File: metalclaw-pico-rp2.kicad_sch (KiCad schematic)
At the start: 115 parts, among them J1 USB_C_Receptacle_USB2.0_14P, J2 Conn_02x05_Odd_Even, SW1 SW_Push, SW2 SW_Push, U1 XC6220B331MR, U2 RP2354B, U3 APS6404L-3SQRx-SN, Y1 XRCGB40M000F1S2FR0

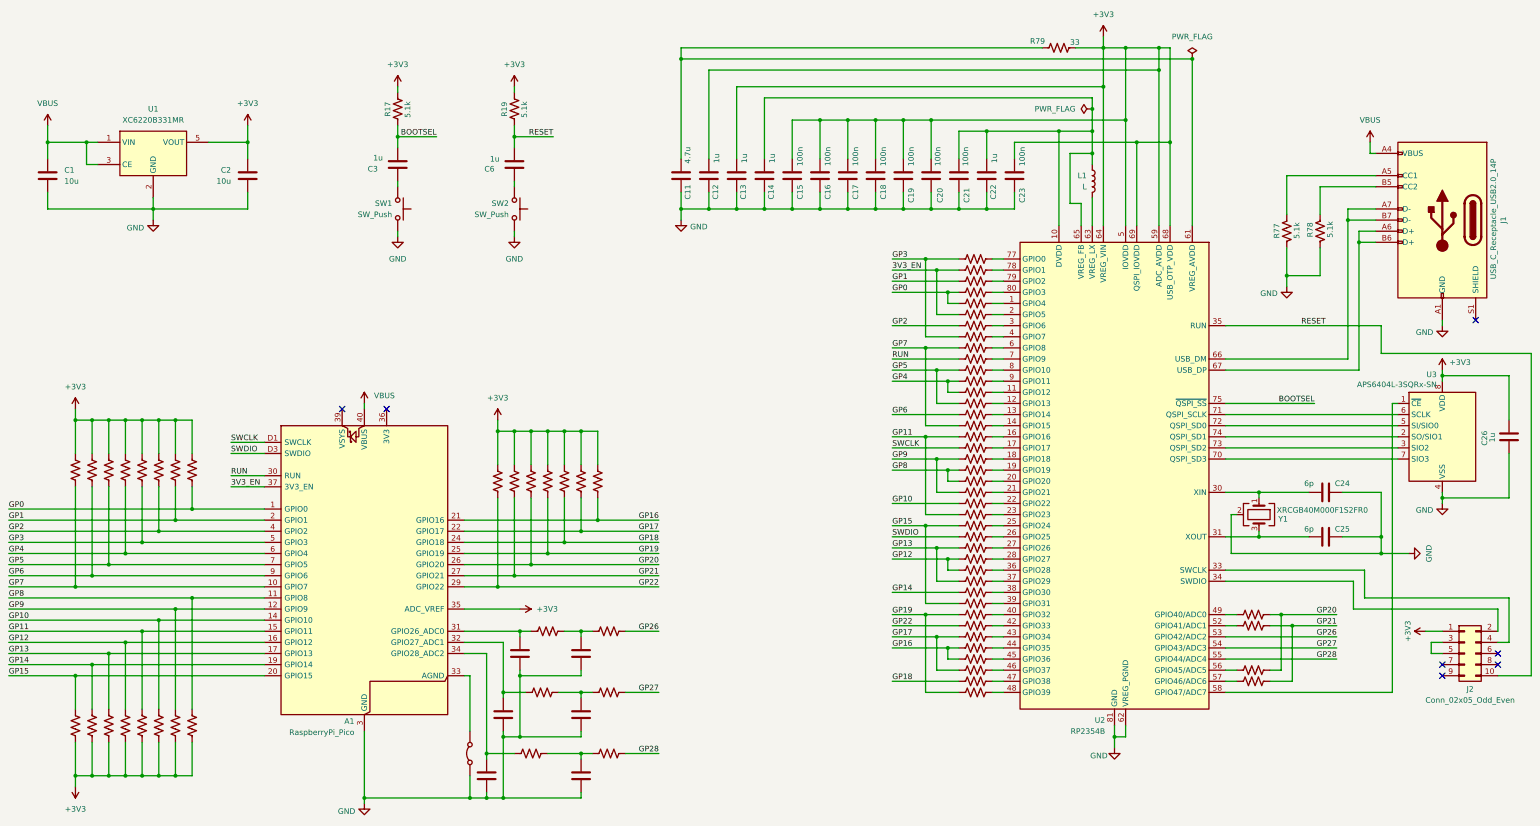
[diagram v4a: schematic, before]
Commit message: Fix power supply connections
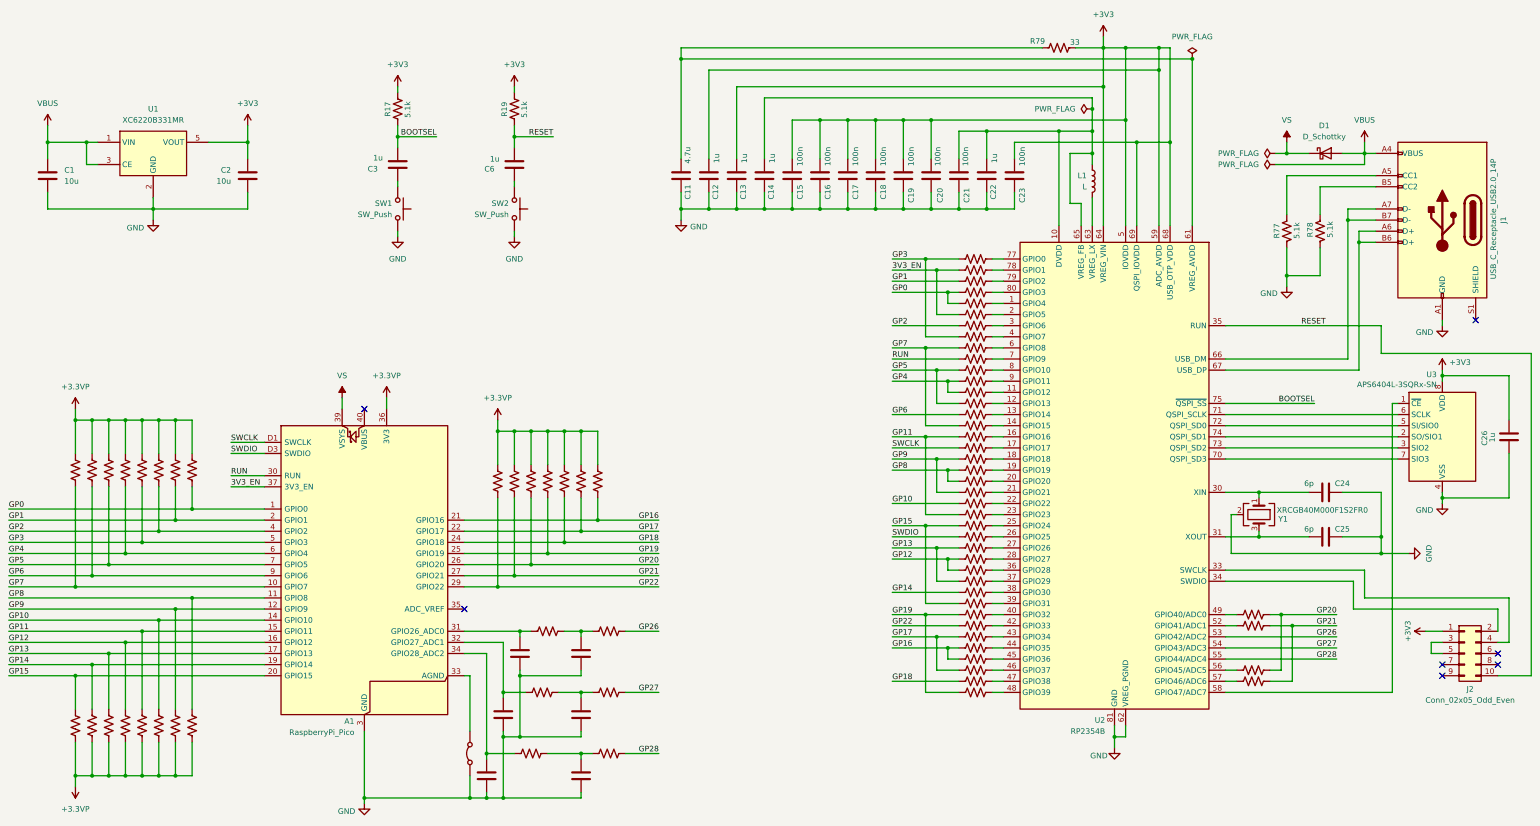
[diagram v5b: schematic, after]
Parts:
- added D1: D_Schottky, symbol Device:D_Schottky
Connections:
- net +3V3: no longer A1.35 (ADC_VREF), R1.2, R10.1, R11.2, R12.1, R13.2, R14.1, R15.2, R16.1, R18.2, R2.1, R20.2, R21.2, R24.2, R26.2, R27.2, R28.2, R3.2, R4.1, R5.2, R6.1, R7.2, R8.1, R9.2
- net VBUS: now also D1.2 (A); no longer A1.40 (VBUS)
- net +3.3VP: now reaches A1.36 (3V3)
- net +3.3VP: now also R1.2, R10.1, R11.2, R12.1, R13.2, R14.1, R15.2, R16.1, R18.2, R2.1, R20.2, R21.2, R24.2, R26.2, R27.2, R28.2, R3.2, R4.1, R5.2, R6.1, R7.2, R8.1, R9.2
- net VS: now reaches A1.39 (VSYS)
- net VS: now also D1.1 (K)

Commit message: Add pull-up for PSRAM chip-select
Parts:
- added R76: 220, Resistor_SMD:R_0201_0603Metric, symbol Device:R_US
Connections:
- net +3V3: now also R76.2
- net at U2.58 (GPIO47/ADC7), U3.1 (~{CE}): now also R76.1
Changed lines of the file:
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@@
 	)
 	(junction
+		(at 353.06 196.85)
+		(diameter 0)
+		(color 0 0 0 0)
+	)
+	(junction
 		(at 241.3 66.04)
 		(diameter 0)
@@
 	(wire
 		(pts
+			(xy 353.06 196.85) (xy 359.41 196.85)
+		)
+		(stroke
+			(width 0)
+			(type default)
+		)
+	)
+	(wire
+		(pts
 			(xy 255.27 184.15) (xy 245.11 184.15)
 		)
@@
 	(wire
 		(pts
+			(xy 353.06 185.42) (xy 353.06 186.69)
+		)
+		(stroke
+			(width 0)
+			(type default)
+		)
+	)
+	(wire
+		(pts
 			(xy 347.98 151.13) (xy 356.87 151.13)
 		)
@@
 	(wire
 		(pts
+			(xy 353.06 194.31) (xy 353.06 196.85)
+		)
+		(stroke
+			(width 0)
+			(type default)
+		)
+	)
+	(wire
+		(pts
 			(xy 73.66 182.88) (xy 73.66 200.66)
 		)
@@
 	(wire
 		(pts
-			(xy 321.31 196.85) (xy 359.41 196.85)
+			(xy 321.31 196.85) (xy 353.06 196.85)
 		)
 		(stroke
@@
 	)
 	(symbol
+		(lib_id "power:+3V3")
+		(at 353.06 185.42 0)
+		(unit 1)
+		(exclude_from_sim no)
+		(in_bom yes)
+		(on_board yes)
+		(dnp no)
+		(property "Reference" "#PWR025"
+			(at 353.06 189.23 0)
+			(effects
+				(font
+					(size 1.27 1.27)
+				)
+				(hide yes)
+			)
+		)
+		(property "Value" "+3V3"
+			(at 353.06 181.356 0)
+			(effects
+				(font
+					(size 1.27 1.27)
+				)
+			)
+		)
+		(property "Footprint" ""
+			(at 353.06 185.42 0)
+			(effects
+				(font
+					(size 1.27 1.27)
+				)
+				(hide yes)
+			)
+		)
+		(property "Datasheet" ""
+			(at 353.06 185.42 0)
+			(effects
+				(font
+					(size 1.27 1.27)
+				)
+				(hide yes)
+			)
+		)
+		(property "Description" "Power symbol creates a global label with name \"+3V3\""
+			(at 353.06 185.42 0)
+			(effects
+				(font
+					(size 1.27 1.27)
+				)
+				(hide yes)
+			)
+		)
+		(pin "1"
+		)
+		(instances
+			(project "metalclaw-pico-rp2"
+				(path "/c83ebc88-59c8-491c-acdb-d3cfac2d55f0"
+					(reference "#PWR025")
+					(unit 1)
+				)
+			)
+		)
+	)
+	(symbol
 		(lib_id "Connector:USB_C_Receptacle_USB2.0_14P")
 		(at 370.84 88.9 0)
@@
 					(unit 1)
 				)
+			)
+		)
+	)
+	(symbol
+		(lib_id "Device:R_US")
+		(at 353.06 190.5 180)
+		(unit 1)
+		(exclude_from_sim no)
+		(in_bom yes)
+		(on_board yes)
+		(dnp no)
+		(property "Reference" "R76"
+			(at 351.79 191.516 0)
+			(effects
+				(font
+					(size 1.27 1.27)
+				)
+				(justify left)
+				(hide yes)
+			)
+		)
+		(property "Value" "220"
+			(at 351.79 188.976 0)
+			(effects
+				(font
+					(size 1.27 1.27)
+				)
+				(justify left)
+				(hide yes)
+			)
+		)
+		(property "Footprint" "Resistor_SMD:R_0201_0603Metric"
+			(at 352.044 190.246 90)
+			(effects
+				(font
+					(size 1.27 1.27)
+				)
+				(hide yes)
+			)
+		)
+		(property "Datasheet" "~"
+			(at 353.06 190.5 0)
+			(effects
+				(font
+					(size 1.27 1.27)
+				)
+				(hide yes)
+			)
+		)
+		(property "Description" "Resistor, US symbol"
+			(at 353.06 190.5 0)
+			(effects
+				(font
+					(size 1.27 1.27)
+				)
+				(hide yes)
+			)
+		)
+		(property "Mouser" "603-AC0201FR-13220RL "
+			(at 353.06 190.5 0)
+			(effects
+				(font
+					(size 1.27 1.27)
+				)
+				(hide yes)
+			)
+		)
+		(pin "1"
+		)
+		(pin "2"
+		)
+		(instances
+			(project "metalclaw-pico-rp2"
+				(path "/c83ebc88-59c8-491c-acdb-d3cfac2d55f0"
+					(reference "R76")
+					(unit 1)
+				)

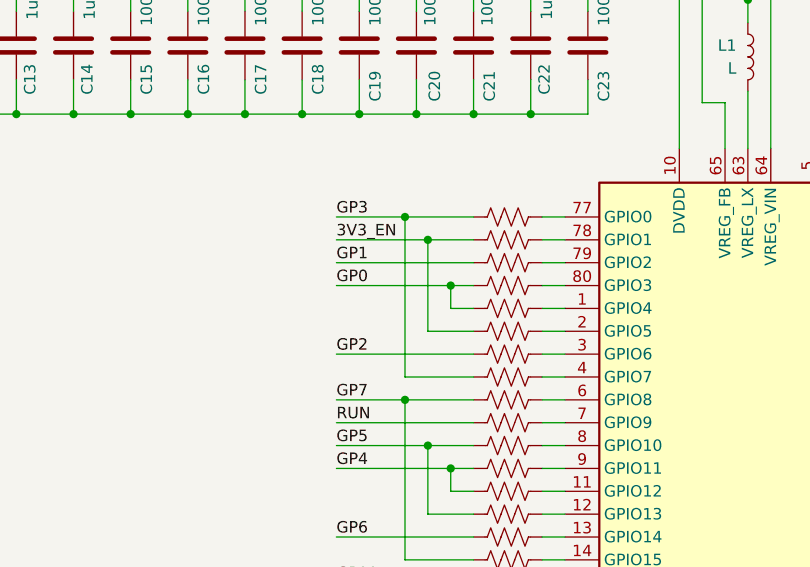
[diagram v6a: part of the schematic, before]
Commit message: Connect GP5 with GP1
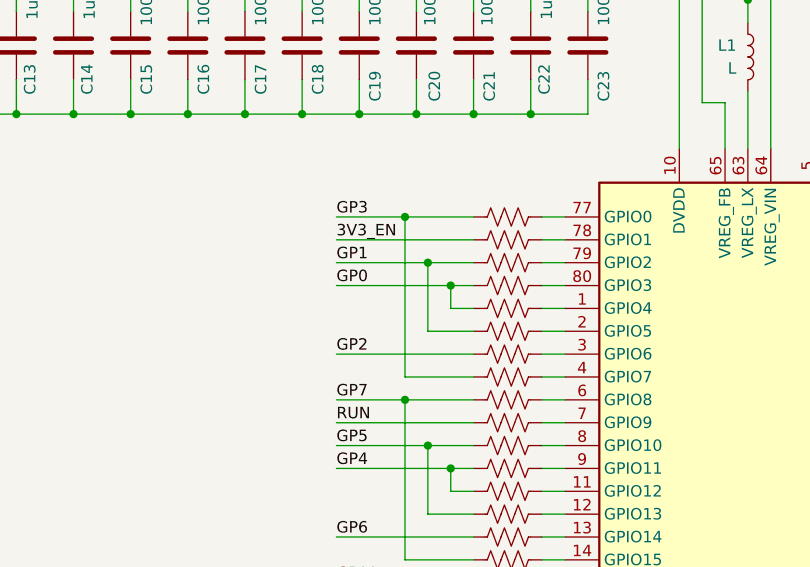
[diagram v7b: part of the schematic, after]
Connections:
- net 3V3_EN: no longer R37.1
- net GP1: now also R37.1
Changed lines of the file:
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@@
 	)
 	(junction
+		(at 255.27 102.87)
+		(diameter 0)
+		(color 0 0 0 0)
+	)
+	(junction
 		(at 81.28 157.48)
 		(diameter 0)
@@
 	)
 	(junction
-		(at 255.27 100.33)
-		(diameter 0)
-		(color 0 0 0 0)
-	)
-	(junction
 		(at 156.21 196.85)
 		(diameter 0)
@@
 	(wire
 		(pts
-			(xy 260.35 100.33) (xy 255.27 100.33)
-		)
-		(stroke
-			(width 0)
-			(type default)
-		)
-	)
-	(wire
-		(pts
 			(xy 228.6 66.04) (xy 234.95 66.04)
 		)
@@
 	(wire
 		(pts
-			(xy 260.35 102.87) (xy 245.11 102.87)
+			(xy 260.35 102.87) (xy 255.27 102.87)
+		)
+		(stroke
+			(width 0)
+			(type default)
+		)
+	)
+	(wire
+		(pts
+			(xy 255.27 102.87) (xy 255.27 110.49)
 		)
 		(stroke
@@
 	(wire
 		(pts
+			(xy 255.27 102.87) (xy 245.11 102.87)
+		)
+		(stroke
+			(width 0)
+			(type default)
+		)
+	)
+	(wire
+		(pts
 			(xy 335.28 101.6) (xy 335.28 104.14)
 		)
@@
 	(wire
 		(pts
-			(xy 255.27 100.33) (xy 245.11 100.33)
+			(xy 245.11 100.33) (xy 260.35 100.33)
 		)
 		(stroke
@@
 		)
 		(stroke
-			(width 0)
-			(type default)
-		)
-	)
-	(wire
-		(pts
-			(xy 255.27 100.33) (xy 255.27 110.49)
-		)
-		(stroke

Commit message: Fix reset circuit
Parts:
- removed C3: 1u, Capacitor_SMD:C_0201_0603Metric, symbol Device:C
- added R80: 5.1k, Resistor_SMD:R_0201_0603Metric, symbol Device:R_US
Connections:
- net BOOTSEL: now also R80.1
- net GND: now also C6.1
- net RESET: now also SW2.2
- net at SW1.2: now also R80.2
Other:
- moved on the sheet: C6, R17, R19, SW1, SW2
